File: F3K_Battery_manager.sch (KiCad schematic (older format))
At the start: 0 parts

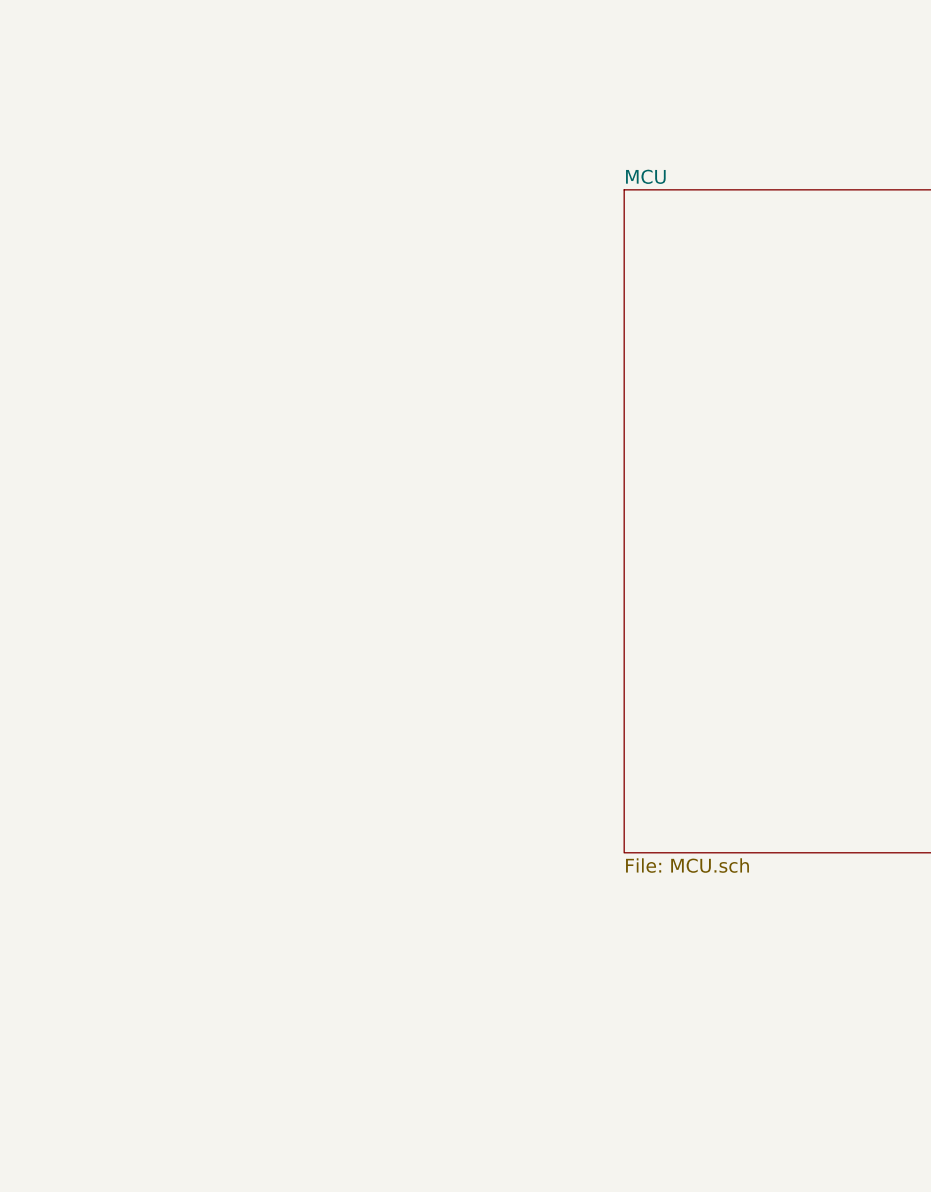
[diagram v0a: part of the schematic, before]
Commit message: Added Hall efect switch
DRV5032
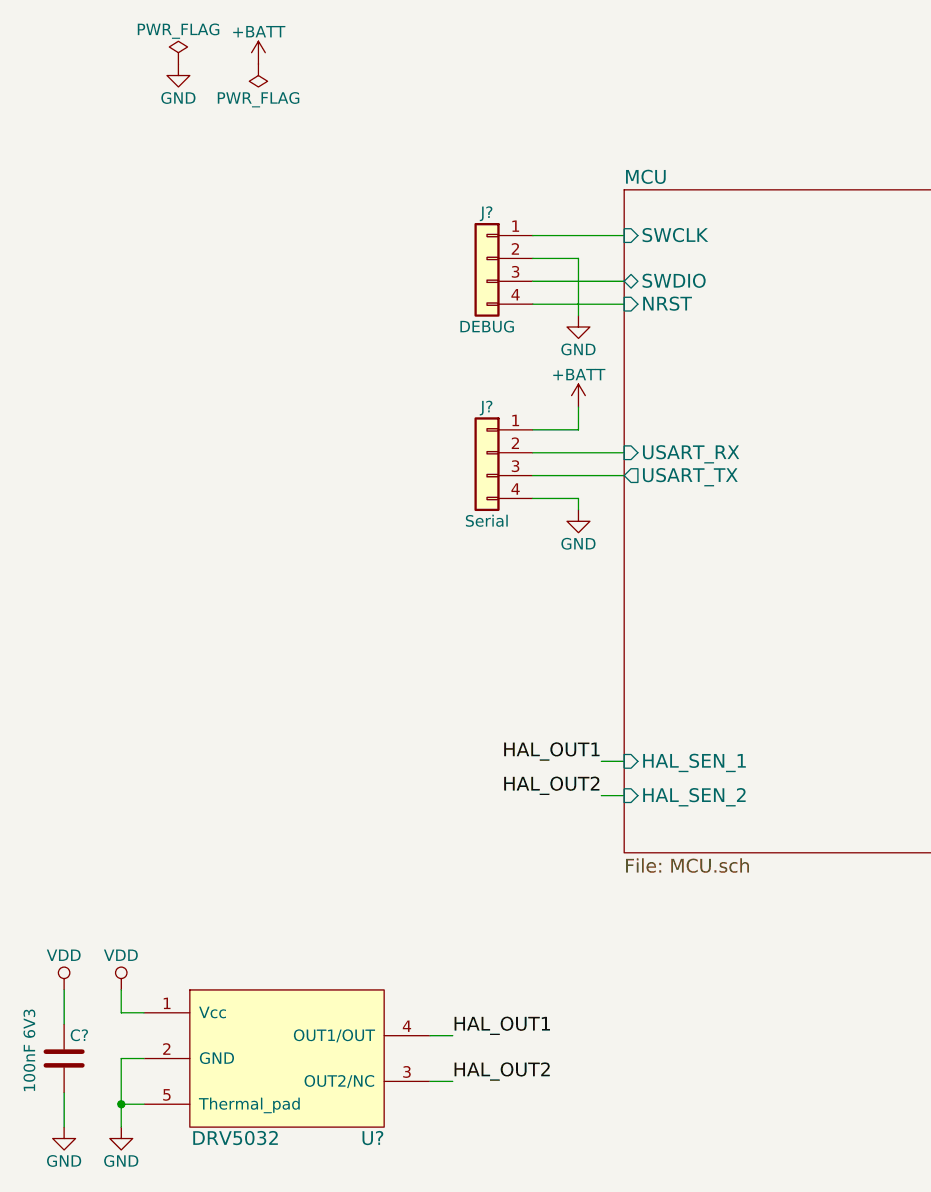
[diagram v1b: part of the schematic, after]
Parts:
- added C?: 100nF 6V3, symbol C
- added J?: DEBUG, symbol Conn_01x04
- added J?: Serial, symbol Conn_01x04
- added U?: DRV5032, lakotamm-sensor:X2SON_4_1.10x1.40mm, symbol DRV5032
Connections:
- new net +BATT: J?.1 (Pin_1)
- new net GND: C?.2, J?.2 (Pin_2), J?.4 (Pin_4), U?.2 (GND), U?.5 (Thermal_pad)
- new net HAL_OUT1: U?.4 (OUT1/OUT)
- new net HAL_OUT2: U?.3 (OUT2/NC)
- new net MCU/NRST: J?.4 (Pin_4)
- new net MCU/SWCLK: J?.1 (Pin_1)
- new net MCU/SWDIO: J?.3 (Pin_3)
- new net MCU/USART_RX: J?.2 (Pin_2)
- new net MCU/USART_TX: J?.3 (Pin_3)
- new net VDD: C?.1, U?.1 (Vcc)
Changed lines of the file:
@@
 LIBS:lakotamm-microprocessors
 LIBS:lakotamm-powersupply
+LIBS:lakotamm-sensor
+LIBS:F3K_Battery_manager-cache
 EELAYER 25 0
 EELAYER END
@@
 F0 "MCU" 60
 F1 "MCU.sch" 60
+F2 "NRST" I L 5900 2600 60
+F3 "SWCLK" I L 5900 2300 60
+F4 "SWDIO" B L 5900 2500 60
+F5 "USART_TX" O L 5900 3350 60
+F6 "USART_RX" I L 5900 3250 60
+F7 "HAL_SEN_1" I L 5900 4600 60
+F8 "HAL_SEN_2" I L 5900 4750 60
 $EndSheet
+$Comp
+L Conn_01x04 J?
+U 1 1 5AA070CB
+P 5300 2400
+F 0 "J?" H 5300 2600 50  0000 C CNN
+F 1 "DEBUG" H 5300 2100 50  0000 C CNN
+F 2 "" H 5300 2400 50  0001 C CNN
+F 3 "" H 5300 2400 50  0001 C CNN
+	1    5300 2400
+	-1   0    0    -1
+$EndComp
+$Comp
+L GND #PWR?
+U 1 1 5AA0735F
+P 5700 2650
+F 0 "#PWR?" H 5700 2400 50  0001 C CNN
+F 1 "GND" H 5700 2500 50  0000 C CNN
+F 2 "" H 5700 2650 50  0001 C CNN
+F 3 "" H 5700 2650 50  0001 C CNN
+	1    5700 2650
+	1    0    0    -1
+$EndComp
+$Comp
+L Conn_01x04 J?
+U 1 1 5AA075F4
+P 5300 3250
+F 0 "J?" H 5300 3450 50  0000 C CNN
+F 1 "Serial" H 5300 2950 50  0000 C CNN
+F 2 "" H 5300 3250 50  0001 C CNN
+F 3 "" H 5300 3250 50  0001 C CNN
+	1    5300 3250
+	-1   0    0    -1
+$EndComp
+$Comp
+L GND #PWR?
+U 1 1 5AA07C91
+P 5700 3500
+F 0 "#PWR?" H 5700 3250 50  0001 C CNN
+F 1 "GND" H 5700 3350 50  0000 C CNN
+F 2 "" H 5700 3500 50  0001 C CNN
+F 3 "" H 5700 3500 50  0001 C CNN
+	1    5700 3500
+	1    0    0    -1
+$EndComp
+$Comp
+L +BATT #PWR?
+U 1 1 5AA081FC
+P 5700 3050
+F 0 "#PWR?" H 5700 2900 50  0001 C CNN
+F 1 "+BATT" H 5700 3190 50  0000 C CNN
+F 2 "" H 5700 3050 50  0001 C CNN
+F 3 "" H 5700 3050 50  0001 C CNN
+	1    5700 3050
+	1    0    0    -1
+$EndComp
+$Comp
+L DRV5032 U?
+U 1 1 5AA08B55
+P 4450 5900
+F 0 "U?" H 4800 5550 60  0000 C CNN
+F 1 "DRV5032" H 4200 5550 60  0000 C CNN
+F 2 "lakotamm-sensor:X2SON_4_1.10x1.40mm" H 4500 5450 60  0001 C CNN
+F 3 "http://www.ti.com/lit/ds/symlink/drv5032.pdf" H 4450 5350 60  0001 C CNN
+	1    4450 5900
+	1    0    0    -1
+$EndComp
+$Comp
+L C C?
+U 1 1 5AA08E27
+P 3450 5900
+F 0 "C?" H 3475 6000 50  0000 L CNN
+F 1 "100nF 6V3" V 3300 5750 50  0000 L CNN
+F 2 "" H 3488 5750 50  0001 C CNN
+F 3 "" H 3450 5900 50  0001 C CNN
+	1    3450 5900
+	1    0    0    -1
+$EndComp
+Wire Wire Line
+	5500 2300 5900 2300
+Wire Wire Line
+	5500 2400 5700 2400
+Wire Wire Line
+	5700 2400 5700 2650
+Wire Wire Line
+	5500 2500 5900 2500
+Wire Wire Line
+	5500 2600 5900 2600
+Wire Wire Line
+	5900 3250 5500 3250
+Wire Wire Line
+	5500 3350 5900 3350
+Wire Wire Line
+	5500 3450 5700 3450
+Wire Wire Line
+	5700 3450 5700 3500
+Wire Wire Line
+	5500 3150 5700 3150
+Wire Wire Line
+	5700 3150 5700 3050
+$Comp
+L GND #PWR?
+U 1 1 5AA09559
+P 3700 6200
+F 0 "#PWR?" H 3700 5950 50  0001 C CNN
+F 1 "GND" H 3700 6050 50  0000 C CNN
+F 2 "" H 3700 6200 50  0001 C CNN
+F 3 "" H 3700 6200 50  0001 C CNN
+	1    3700 6200
+	1    0    0    -1
+$EndComp
+Wire Wire Line
+	3800 5900 3700 5900
+Wire Wire Line
+	3700 5900 3700 6200
+Wire Wire Line
+	3800 6100 3700 6100
+Connection ~ 3700 6100
+$Comp
+L VDD #PWR?
+U 1 1 5AA0982A
+P 3700 5600
+F 0 "#PWR?" H 3700 5450 50  0001 C CNN
+F 1 "VDD" H 3700 5750 50  0000 C CNN
+F 2 "" H 3700 5600 50  0001 C CNN
+F 3 "" H 3700 5600 50  0001 C CNN
+	1    3700 5600
+	1    0    0    -1
+$EndComp
+Wire Wire Line
+	3700 5600 3700 5700
+Wire Wire Line
+	3700 5700 3800 5700
+$Comp
+L VDD #PWR?
+U 1 1 5AA09936
+P 3450 5600
+F 0 "#PWR?" H 3450 5450 50  0001 C CNN
+F 1 "VDD" H 3450 5750 50  0000 C CNN
+F 2 "" H 3450 5600 50  0001 C CNN
+F 3 "" H 3450 5600 50  0001 C CNN
+	1    3450 5600
+	1    0    0    -1
+$EndComp
+$Comp
+L GND #PWR?
+U 1 1 5AA0996B
+P 3450 6200
+F 0 "#PWR?" H 3450 5950 50  0001 C CNN
+F 1 "GND" H 3450 6050 50  0000 C CNN
+F 2 "" H 3450 6200 50  0001 C CNN
+F 3 "" H 3450 6200 50  0001 C CNN
+	1    3450 6200
+	1    0    0    -1
+$EndComp
+Wire Wire Line
+	3450 5600 3450 5750
+Wire Wire Line
+	3450 6050 3450 6200
+Text Label 5150 5800 0    60   ~ 0
+HAL_OUT1
+Wire Wire Line
+	5050 5800 5150 5800
+Text Label 5150 6000 0    60   ~ 0
+HAL_OUT2
+Wire Wire Line
+	5050 6000 5150 6000
+Text Label 5800 4600 2    60   ~ 0
+HAL_OUT1
+Wire Wire Line
+	5800 4600 5900 4600
+Text Label 5800 4750 2    60   ~ 0
+HAL_OUT2
+Wire Wire Line
+	5800 4750 5900 4750
+$Comp
+L PWR_FLAG #FLG?
+U 1 1 5AA0B07D
+P 3950 1550
+F 0 "#FLG?" H 3950 1625 50  0001 C CNN
+F 1 "PWR_FLAG" H 3950 1700 50  0000 C CNN
+F 2 "" H 3950 1550 50  0001 C CNN
+F 3 "" H 3950 1550 50  0001 C CNN
+	1    3950 1550
+	1    0    0    -1
+$EndComp
+$Comp
+L GND #PWR?
+U 1 1 5AA0B18B
+P 3950 1550
+F 0 "#PWR?" H 3950 1300 50  0001 C CNN
+F 1 "GND" H 3950 1400 50  0000 C CNN
+F 2 "" H 3950 1550 50  0001 C CNN
+F 3 "" H 3950 1550 50  0001 C CNN
+	1    3950 1550
+	1    0    0    -1
+$EndComp
+$Comp
+L PWR_FLAG #FLG?
+U 1 1 5AA0B25E
+P 4300 1550
+F 0 "#FLG?" H 4300 1625 50  0001 C CNN
+F 1 "PWR_FLAG" H 4300 1700 50  0000 C CNN
+F 2 "" H 4300 1550 50  0001 C CNN
+F 3 "" H 4300 1550 50  0001 C CNN
+	1    4300 1550
+	-1   0    0    1
+$EndComp
+$Comp
+L +BATT #PWR?
+U 1 1 5AA0B29D
+P 4300 1550
+F 0 "#PWR?" H 4300 1400 50  0001 C CNN
+F 1 "+BATT" H 4300 1690 50  0000 C CNN
+F 2 "" H 4300 1550 50  0001 C CNN
+F 3 "" H 4300 1550 50  0001 C CNN
+	1    4300 1550
+	1    0    0    -1
+$EndComp
 $EndSCHEMATC

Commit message: Added Buzzer
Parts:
- added BZ?: Buzzer, symbol Buzzer
- added Q?: CSD13380F3, symbol CSD13380F3
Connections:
- wire segments 22 -> 28
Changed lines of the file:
@@
 LIBS:lakotamm-powersupply
 LIBS:lakotamm-sensor
+LIBS:lakotamm-transistor
 LIBS:F3K_Battery_manager-cache
 EELAYER 25 0
@@
 F7 "HAL_SEN_1" I L 5900 4600 60
 F8 "HAL_SEN_2" I L 5900 4750 60
+F9 "BUZZER" O R 7650 2850 60
 $EndSheet
 $Comp
@@
 	1    0    0    -1
 $EndComp
+$Comp
+L Buzzer BZ?
+U 1 1 5AA0FFE4
+P 8400 2500
+F 0 "BZ?" H 8550 2550 50  0000 L CNN
+F 1 "Buzzer" H 8550 2450 50  0000 L CNN
+F 2 "" V 8375 2600 50  0001 C CNN
+F 3 "" V 8375 2600 50  0001 C CNN
+	1    8400 2500
+	1    0    0    -1
+$EndComp
+$Comp
+L CSD13380F3 Q?
+U 1 1 5AA10AB6
+P 8150 2850
+F 0 "Q?" H 8350 2925 50  0000 L CNN
+F 1 "CSD13380F3" H 8350 2850 50  0000 L CNN
+F 2 "" H 8350 2775 50  0001 L CIN
+F 3 "http://www.ti.com/product/CSD13380F3" H 7450 2550 50  0001 L CNN
+	1    8150 2850
+	1    0    0    -1
+$EndComp
+$Comp
+L VDD #PWR?
+U 1 1 5AA11015
+P 8250 2300
+F 0 "#PWR?" H 8250 2150 50  0001 C CNN
+F 1 "VDD" H 8250 2450 50  0000 C CNN
+F 2 "" H 8250 2300 50  0001 C CNN
+F 3 "" H 8250 2300 50  0001 C CNN
+	1    8250 2300
+	1    0    0    -1
+$EndComp
+Wire Wire Line
+	8250 2300 8250 2400
+Wire Wire Line
+	8250 2400 8300 2400
+Wire Wire Line
+	8300 2600 8250 2600
+Wire Wire Line
+	8250 2600 8250 2650
+$Comp
+L GND #PWR?
+U 1 1 5AA112B0
+P 8250 3100
+F 0 "#PWR?" H 8250 2850 50  0001 C CNN
+F 1 "GND" H 8250 2950 50  0000 C CNN
+F 2 "" H 8250 3100 50  0001 C CNN
+F 3 "" H 8250 3100 50  0001 C CNN
+	1    8250 3100
+	1    0    0    -1
+$EndComp
+Wire Wire Line
+	8250 3050 8250 3100
+Wire Wire Line
+	7650 2850 7950 2850
 $EndSCHEMATC

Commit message: Added Boost converter
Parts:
- removed J?: Serial, symbol Conn_01x04
- added J?: Conn_01x03, symbol Conn_01x03
- added J?: Serial, symbol Conn_01x03
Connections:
- net labels added: LPUART_TX
- net labels removed: HAL_OUT1, HAL_OUT2
- wire segments 28 -> 35
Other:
- note added: "Hall efect switch\n"
- moved on the sheet: BZ?, C?, J?, U?

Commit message: Added Input for coil and battery
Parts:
- removed Q?: CSD13380F3, symbol CSD13380F3
- added J?: BATT +, symbol Conn_01x01
- added J?: BATT -, symbol Conn_01x01
- added J?: Coil 1, symbol Conn_01x01
- added J?: Coil 2, symbol Conn_01x01
- added Q? (x2): CSD13385F5, symbol CSD13385F5
- added R?: 680R, symbol R
- added R?: 12k, symbol R
- BZ?: MPN (none) -> ST-0402T
- C?: value 100nF 6V3 -> 2u2 6V3
- J?: value Conn_01x03 -> Receiver
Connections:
- net labels added: USART_TX
- net labels removed: LPUART_TX
- wire segments 35 -> 51
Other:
- moved on the sheet: BZ?, C?, J?, U?

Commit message: small updates
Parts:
- U?: MPN (none) -> DRV5032FD
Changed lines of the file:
@@
 LIBS:power
 LIBS:device
-LIBS:switches
-LIBS:relays
-LIBS:motors
-LIBS:transistors
-LIBS:conn
 LIBS:linear
 LIBS:regul
-LIBS:74xx
-LIBS:cmos4000
 LIBS:adc-dac
 LIBS:memory
@@
 LIBS:digital-audio
 LIBS:philips
-LIBS:display
 LIBS:cypress
 LIBS:siliconi
@@
 LIBS:atmel
 LIBS:contrib
-LIBS:valves
 LIBS:lakotamm-microprocessors
 LIBS:lakotamm-powersupply
@@
 LIBS:lakotamm-transistor
 LIBS:lakotamm-wireless
+LIBS:MCU_ST_STM32
+LIBS:Transistor
+LIBS:Connector
 LIBS:F3K_Battery_manager-cache
 EELAYER 25 0
@@
 F7 "HAL_SEN_2" I L 4850 5800 60
 F8 "BUZZER" O R 6600 2700 60
-F9 "Control_OUT1" O R 6600 3900 60
-F10 "Control_OUT2" O R 6600 4000 60
-F11 "ENA" O R 6600 4200 60
-F12 "OUT_Voltage" I R 6600 4400 60
-F13 "OUT_Current" I R 6600 4500 60
-F14 "BATT_Voltage" I L 4850 4150 60
-F15 "USART_TX" B L 4850 3200 60
+F9 "Control_OUT" O R 6600 4000 60
+F10 "ENA" O R 6600 4200 60
+F11 "OUT_Voltage" I R 6600 4400 60
+F12 "OUT_Current" I R 6600 4500 60
+F13 "BATT_Voltage" I L 4850 4150 60
+F14 "USART_TX" B L 4850 3200 60
 $EndSheet
 $Comp
@@
 F 2 "lakotamm-sensor:X2SON_4_1.10x1.40mm" H 3900 5250 60  0001 C CNN
 F 3 "http://www.ti.com/lit/ds/symlink/drv5032.pdf" H 3850 5150 60  0001 C CNN
+F 4 "DRV5032FD" H 3850 5700 60  0001 C CNN "MPN"
 	1    3850 5700
 	1    0    0    -1
@@
 F1 "boost_converter.sch" 60
 F2 "VOUT" O R 9150 4000 60
-F3 "Control_OUT1" I L 7100 3900 60
-F4 "Control_OUT2" I L 7100 4000 60
-F5 "ENA" I L 7100 4200 60
-F6 "OUT_Current" O L 7100 4400 60
-F7 "OUT_Voltage" O L 7100 4500 60
+F3 "Control_OUT" I L 7100 4000 60
+F4 "ENA" I L 7100 4200 60
+F5 "OUT_Current" O L 7100 4400 60
+F6 "OUT_Voltage" O L 7100 4500 60
 $EndSheet
 Wire Wire Line
@@
 Wire Wire Line
 	6600 4000 7100 4000
-Wire Wire Line
-	6600 3900 7100 3900
 $Comp
 L Conn_01x03 J?
